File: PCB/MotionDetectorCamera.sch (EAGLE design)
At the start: 163 parts, among them J1 S-MOUNT-LENS-HOLDER, J2 MINI-USB-JACK, Q1 PMOS-NEXPERIA-SOT1220, Q2 PMOS-NEXPERIA-SOT1220, Q3 PMOS-NEXPERIA-SOT1220, U1 TI-TPS6280XYKAR, U10 TI-TPS22919DCK, U11 TI-TPS22919DCK, U12 STM-STM32F730, U13 MICROCHIP-MIC550X, U14 TI-MSP430FR2422IRHL, U15 TI-SN74AXC4T774RSV, U16 TI-TPS22919DCK, U17 DIODESINC-DT1446-04V-7, U18 TI-SN74LVC1G126, U19 PANASONIC-EKMB110711X, U2 TI-TPS6280XYKAR, U3 TI-TPS63805YFFR, U4 LATTICE-ICE40HX4K-BG121, U5 ON-AR0330CS1C12SPKA0, U6 ALLIANCE-AS4C8M16MSA-6BIN, U7 MAXIM-MAX40203ANS+T, U8 TI-TPS22919DCK, U9 MICROSD-SOCKET, X1 SITIME-SIT8021, X2 SITIME-SIT8021, X3 EPSON-MC-306

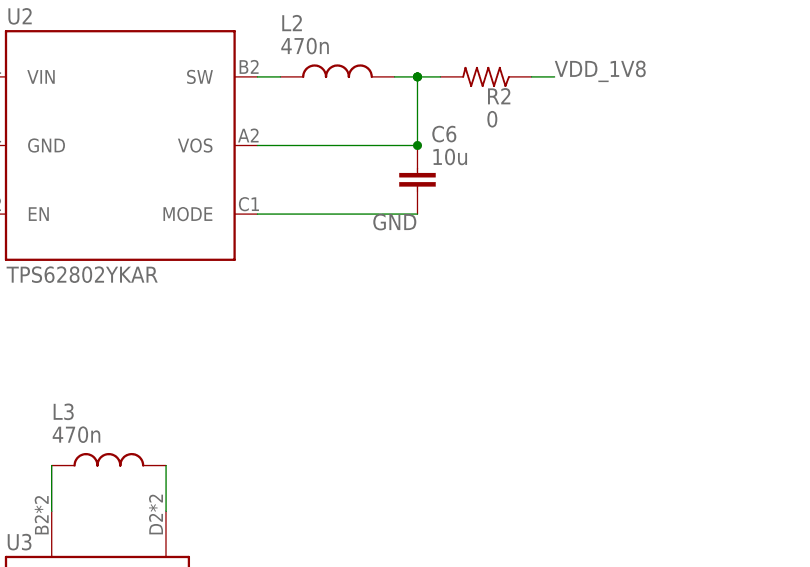
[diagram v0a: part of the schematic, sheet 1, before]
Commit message: Bump 1.8V rail up to 1.9V, so that it's easier to meet the SD card Vih in 3.3V mode
Vih(2.8V) = 0.625*VDD = .625*2.8 = 1.75 V =>
    50mV away from 1.8V rail
    150mV away from 1.9V rail
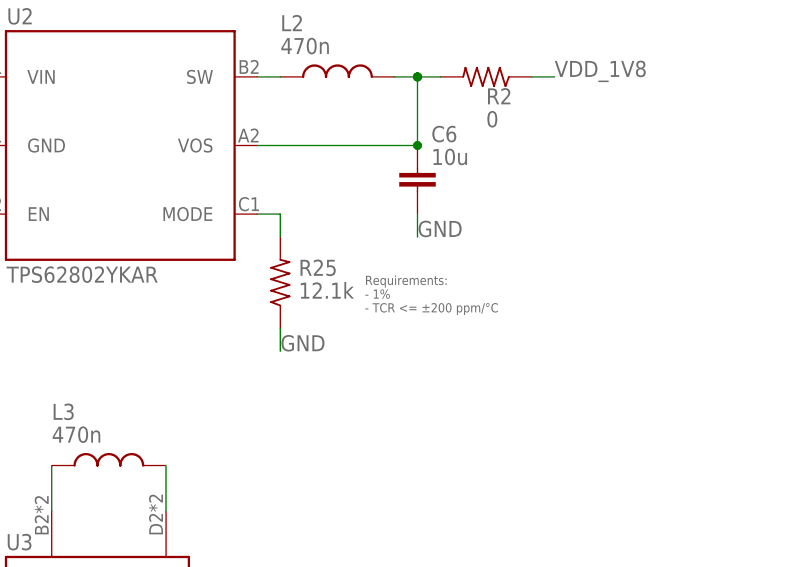
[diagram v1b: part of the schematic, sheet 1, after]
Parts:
- added R25: 12.1k, EagleLibrary:RESISTOR0402
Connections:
- new net N$21: R25.2, U2.MODE
- net GND: now also R25.1; no longer U2.MODE
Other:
- note added: "Requirements: - 1% - TCR <= ±200 ppm/°C"
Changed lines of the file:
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@@
 <attribute name="PN" value="GRM155R61H104KE19D"/>
+</part>
+<part name="R25" library="EagleLibrary" deviceset="RESISTOR" device="0402" value="12.1k">
+<attribute name="MFG" value="Walsin"/>
+<attribute name="PN" value="WR04X1212FTL"/>
 </part>
 </parts>
@@
 <text x="172.974" y="25.146" size="1.016" layer="95" align="top-left">Derated to meet suggested
 1uF @ 5.5V bias</text>
+<text x="179.578" y="257.302" size="1.016" layer="95" align="top-left">Requirements:
+- 1%
+- TCR &lt;= ±200 ppm/°C</text>
 </plain>
 <instances>
@@
 <attribute name="VALUE" x="134.366" y="22.479" size="1.778" layer="96"/>
 <attribute name="MFG" x="114.3" y="30.48" size="1.778" layer="96" display="off"/>
+</instance>
+<instance part="R25" gate="G$1" x="170.18" y="256.54" smashed="yes" rot="R90">
+<attribute name="NAME" x="172.212" y="257.302" size="1.778" layer="95"/>
+<attribute name="VALUE" x="172.212" y="254.762" size="1.778" layer="96"/>
+<attribute name="MFG" x="170.18" y="256.54" size="1.778" layer="96" rot="R90" display="off"/>
+<attribute name="PN" x="170.18" y="256.54" size="1.778" layer="96" rot="R90" display="off"/>
 </instance>
 </instances>
@@
 <wire x1="167.64" y1="309.88" x2="185.42" y2="309.88" width="0.1524" layer="91"/>
 <pinref part="C3" gate="G$1" pin="2"/>
-</segment>
-<segment>
-<pinref part="U2" gate="G$1" pin="MODE"/>
-<label x="185.42" y="264.16" size="1.778" layer="95" align="top-right"/>
-<wire x1="167.64" y1="264.16" x2="185.42" y2="264.16" width="0.1524" layer="91"/>
-<pinref part="C6" gate="G$1" pin="2"/>
 </segment>
 <segment>
@@
 <wire x1="132.08" y1="20.32" x2="132.08" y2="17.78" width="0.1524" layer="91"/>
 <label x="132.08" y="17.78" size="1.778" layer="95" align="bottom-right"/>
+</segment>
+<segment>
+<pinref part="C6" gate="G$1" pin="2"/>
+<wire x1="185.42" y1="264.16" x2="185.42" y2="261.62" width="0.1524" layer="91"/>
+<label x="185.42" y="261.62" size="1.778" layer="95"/>
+</segment>
+<segment>
+<pinref part="R25" gate="G$1" pin="1"/>
+<wire x1="170.18" y1="251.46" x2="170.18" y2="248.92" width="0.1524" layer="91"/>
+<label x="170.18" y="248.92" size="1.778" layer="95"/>
 </segment>
 </net>
@@
 </segment>
 </net>
+<net name="N$21" class="0">
+<segment>
+<pinref part="U2" gate="G$1" pin="MODE"/>
+<wire x1="167.64" y1="264.16" x2="170.18" y2="264.16" width="0.1524" layer="91"/>
+<pinref part="R25" gate="G$1" pin="2"/>
+<wire x1="170.18" y1="264.16" x2="170.18" y2="261.62" width="0.1524" layer="91"/>
+</segment>
+</net>

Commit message: Rename nets 1V8 -> 1V9
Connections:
- net VDD_1V8 renamed VDD_1V9
- net VDD_1V8_IMG renamed VDD_1V9_IMG
- net VDD_1V8_IMG_EN renamed VDD_1V9_IMG_EN
- net VDD_1V8_SD renamed VDD_1V9_SD
- net VDD_1V8_STM renamed VDD_1V9_STM
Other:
- note added: "VDD_1V9"
- note added: "VDD_1V9_IMG"
- note added: "VDD_1V9_STM - Battery: VDD_1V9_STM = HiZ - USB: VDD_1V9_STM = VDD_1V9"
- note added: "VDD_A - Battery: VDD_A = VDD_BAT - USB: VDD_A = 1V9"
- note removed: "VDD_1V8"
- note removed: "VDD_1V8_IMG"
- note removed: "VDD_1V8_STM - Battery: VDD_1V8_STM = HiZ - USB: VDD_1V8_STM = VDD_1V8"
- note removed: "VDD_A - Battery: VDD_A = VDD_BAT - USB: VDD_A = 1V8"
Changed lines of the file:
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@@
 through a via at a different
 layer."</text>
-<text x="12.7" y="81.28" size="3.81" layer="95" align="top-left">VDD_1V8_STM
-- Battery:  VDD_1V8_STM = HiZ
-- USB:      VDD_1V8_STM = VDD_1V8</text>
+<text x="12.7" y="81.28" size="3.81" layer="95" align="top-left">VDD_1V9_STM
+- Battery:  VDD_1V9_STM = HiZ
+- USB:      VDD_1V9_STM = VDD_1V9</text>
 <text x="12.7" y="411.48" size="3.81" layer="95" align="top-left">VDD_A
 - Battery:  VDD_A = VDD_BAT
-- USB:      VDD_A = 1V8</text>
+- USB:      VDD_A = 1V9</text>
 <text x="12.7" y="373.38" size="3.81" layer="95" align="top-left">VDD_B
 - Battery:  VDD_B = HiZ / VDD_BAT
@@
 - USB:      VDD_B = VDD_USB</text>
 <text x="12.7" y="330.2" size="3.81" layer="95" align="top-left">VDD_1V2</text>
-<text x="12.7" y="281.94" size="3.81" layer="95" align="top-left">VDD_1V8</text>
+<text x="12.7" y="281.94" size="3.81" layer="95" align="top-left">VDD_1V9</text>
 <text x="12.7" y="218.44" size="3.81" layer="95" align="top-left">VDD_2V8</text>
 <text x="99.568" y="422.402" size="1.016" layer="95" align="top-left">This PFET serves 2 purposes for the battery power supply:
@@
 <text x="103.886" y="379.984" size="1.016" layer="95" align="top-left">Capacitor helps minimize reverse current spikes
 when battery is inserted with reverse polarity.</text>
-<text x="12.7" y="172.72" size="3.81" layer="95" align="top-left">VDD_1V8_IMG</text>
+<text x="12.7" y="172.72" size="3.81" layer="95" align="top-left">VDD_1V9_IMG</text>
 <text x="12.7" y="142.24" size="3.81" layer="95" align="top-left">VDD_2V8_IMG</text>
 <text x="12.7" y="111.76" size="3.81" layer="95" align="top-left">VDD_2V8_SD</text>
@@
 </segment>
 </net>
-<net name="VDD_1V8" class="0">
+<net name="VDD_1V9" class="0">
 <segment>
 <pinref part="R2" gate="G$1" pin="1"/>
@@
 </segment>
 </net>
-<net name="VDD_1V8_STM" class="0">
+<net name="VDD_1V9_STM" class="0">
 <segment>
 <wire x1="160.02" y1="76.2" x2="162.56" y2="76.2" width="0.1524" layer="91"/>
@@
 </segment>
 </net>
-<net name="VDD_1V8_IMG" class="0">
+<net name="VDD_1V9_IMG" class="0">
 <segment>
 <wire x1="160.02" y1="167.64" x2="162.56" y2="167.64" width="0.1524" layer="91"/>
@@
 </segment>
 </net>
-<net name="VDD_1V8_IMG_EN" class="0">
+<net name="VDD_1V9_IMG_EN" class="0">
 <segment>
 <wire x1="137.16" y1="160.02" x2="134.62" y2="160.02" width="0.1524" layer="91"/>
@@
 </segment>
 </net>
-<net name="VDD_1V8" class="0">
+<net name="VDD_1V9" class="0">
 <segment>
 <pinref part="U15" gate="G$1" pin="VCCB"/>
@@
 </segment>
 </net>
-<net name="VDD_1V8_IMG_EN" class="0">
+<net name="VDD_1V9_IMG_EN" class="0">
 <segment>
 <wire x1="35.56" y1="78.74" x2="33.02" y2="78.74" width="0.1524" layer="91"/>
@@
 </busses>
 <nets>
-<net name="VDD_1V8" class="0">
+<net name="VDD_1V9" class="0">
 <segment>
 <pinref part="C17" gate="G$1" pin="1"/>
@@
 </busses>
 <nets>
-<net name="VDD_1V8_IMG" class="0">
+<net name="VDD_1V9_IMG" class="0">
 <segment>
 <pinref part="U5" gate="A" pin="VDD_IO"/>
@@
 </busses>
 <nets>
-<net name="VDD_1V8" class="0">
+<net name="VDD_1V9" class="0">
 <segment>
 <pinref part="C43" gate="G$1" pin="1"/>
@@
 </busses>
 <nets>
-<net name="VDD_1V8_SD" class="0">
+<net name="VDD_1V9_SD" class="0">
 <segment>
 <pinref part="R22" gate="G$1" pin="2"/>
@@
 </segment>
 </net>
-<net name="VDD_1V8_STM" class="0">
+<net name="VDD_1V9_STM" class="0">
 <segment>
 <pinref part="U12" gate="K" pin="VDD_C5"/>

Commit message: Comments
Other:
- note added: "We're using 1.9V instead of 1.8V purely to help meet the Vih of the SD card when it's in 3.3V mode. In 3.3V mode, the SD card is supposed to be supplied 3.3V signals, but the ICE40 gives it 1.9V signals instead. We're doing this because we haven't found a good method of switching the signal voltage without introducing capacitance on the signalling lines (which can greatly impact the 100MHz high-s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"
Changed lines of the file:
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@@
 - 1%
 - TCR &lt;= ±200 ppm/°C</text>
+<text x="12.7" y="274.32" size="1.016" layer="95" align="top-left">We're using 1.9V instead of 1.8V purely to
+help meet the Vih of the SD card when it's
+in 3.3V mode.
+In 3.3V mode, the SD card is supposed to
+be supplied 3.3V signals, but the ICE40
+gives it 1.9V signals instead. We're doing
+this because we haven't found a good
+method of switching the signal voltage
+without introducing capacitance on the
+signalling lines (which can greatly impact
+the 100MHz high-speed mode).</text>
 </plain>
 <instances>

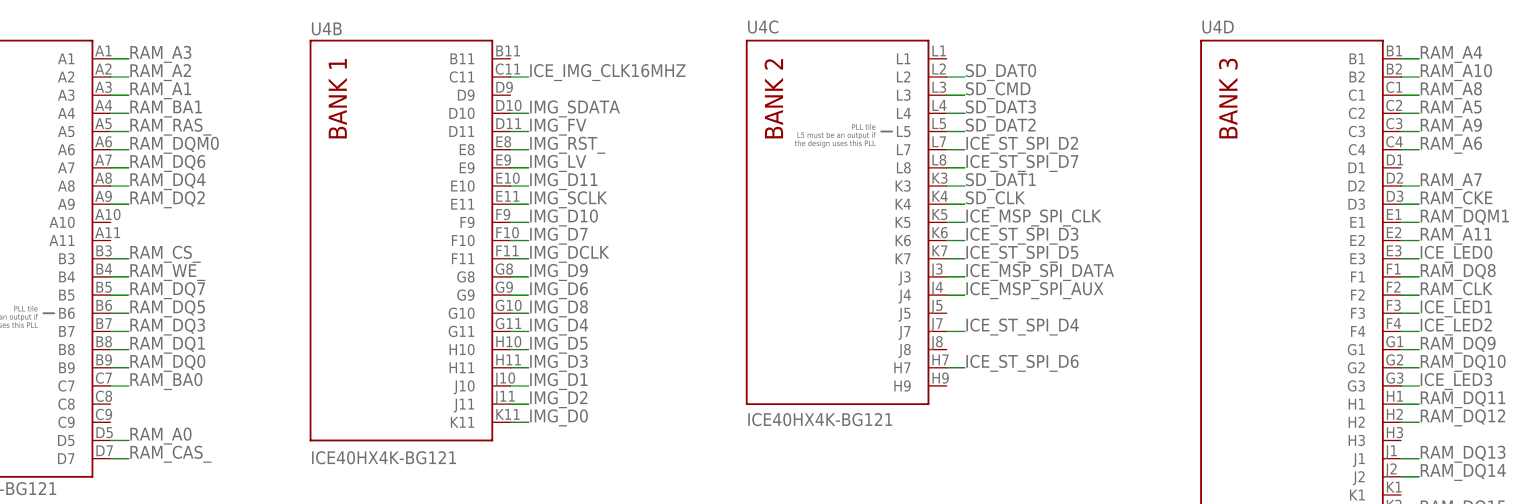
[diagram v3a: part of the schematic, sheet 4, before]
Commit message: Fixed ICE40 PLL tile pins so that they're either unused, or output-only
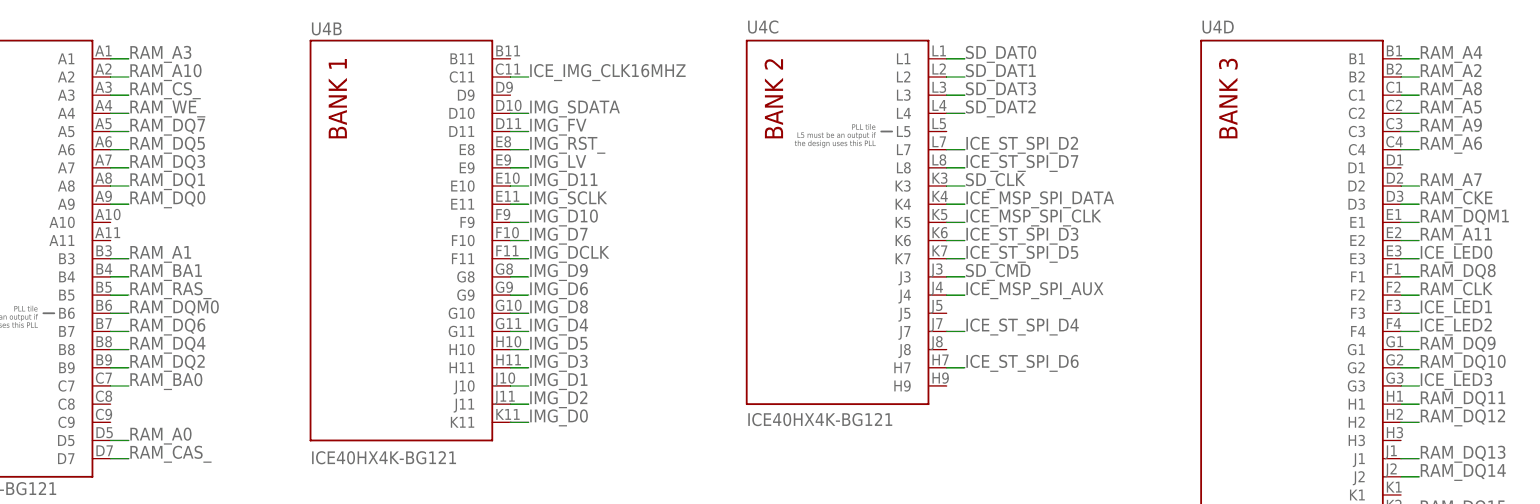
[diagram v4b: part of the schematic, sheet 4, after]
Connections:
- net ICE_MSP_SPI_DATA: now also U4C.K4; no longer U4C.J3
- net RAM_A1: now also U4A.B3; no longer U4A.A3
- net RAM_A10: now also U4A.A2; no longer U4D.B2
- net RAM_A2: now also U4D.B2; no longer U4A.A2
- net RAM_BA1: now also U4A.B4; no longer U4A.A4
- net RAM_CS_: now also U4A.A3; no longer U4A.B3
- net RAM_DQ0: now also U4A.A9; no longer U4A.B9
- net RAM_DQ1: now also U4A.A8; no longer U4A.B8
- net RAM_DQ2: now also U4A.B9; no longer U4A.A9
- net RAM_DQ3: now also U4A.A7; no longer U4A.B7
- net RAM_DQ4: now also U4A.B8; no longer U4A.A8
- net RAM_DQ5: now also U4A.A6; no longer U4A.B6
- net RAM_DQ6: now also U4A.B7; no longer U4A.A7
- net RAM_DQ7: now also U4A.A5; no longer U4A.B5
- net RAM_DQM0: now also U4A.B6; no longer U4A.A6
- net RAM_RAS_: now also U4A.B5; no longer U4A.A5
- net RAM_WE_: now also U4A.A4; no longer U4A.B4
- net SD_CLK: now also U4C.K3; no longer U4C.K4
- net SD_CMD: now also U4C.J3; no longer U4C.L3
- net SD_DAT0: now also U4C.L1; no longer U4C.L2
- net SD_DAT1: now also U4C.L2; no longer U4C.K3
- net SD_DAT2: now also U4C.L4; no longer U4C.L5
- net SD_DAT3: now also U4C.L3; no longer U4C.L4

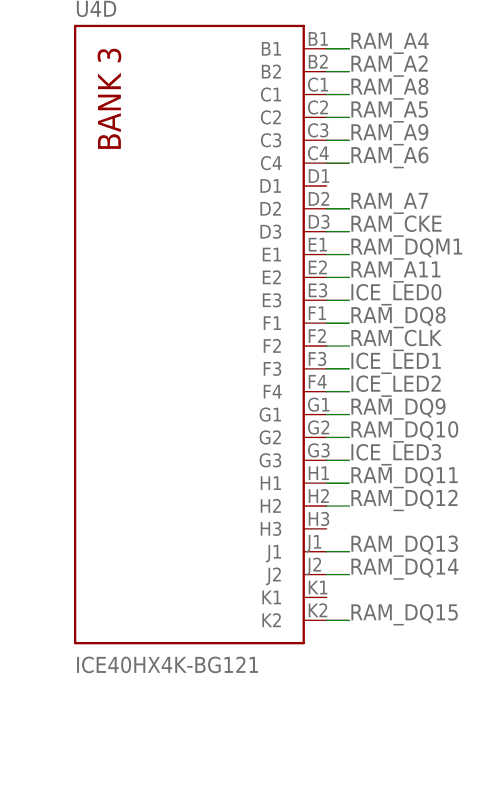
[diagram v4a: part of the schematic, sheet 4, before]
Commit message: Compact wires going to RAM now that we no longer have an A12 net (ball G1)
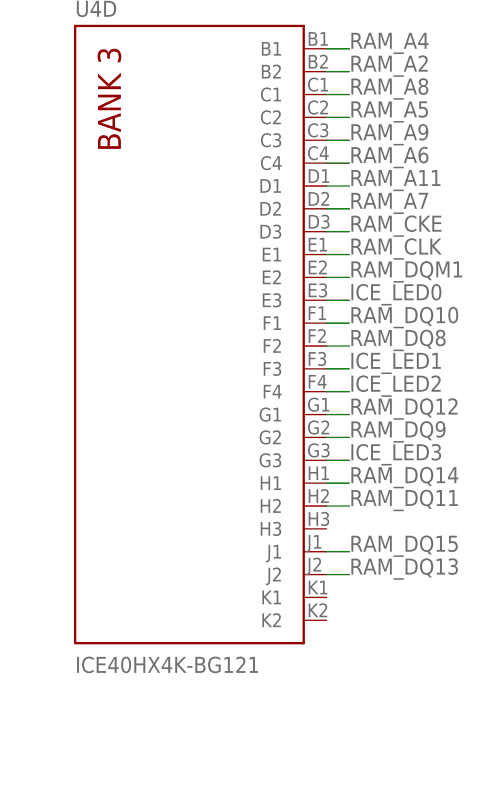
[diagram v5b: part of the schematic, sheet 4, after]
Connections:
- net RAM_A11: now also U4D.D1; no longer U4D.E2
- net RAM_CLK: now also U4D.E1; no longer U4D.F2
- net RAM_DQ10: now also U4D.F1; no longer U4D.G2
- net RAM_DQ11: now also U4D.H2; no longer U4D.H1
- net RAM_DQ12: now also U4D.G1; no longer U4D.H2
- net RAM_DQ13: now also U4D.J2; no longer U4D.J1
- net RAM_DQ14: now also U4D.H1; no longer U4D.J2
- net RAM_DQ15: now also U4D.J1; no longer U4D.K2
- net RAM_DQ8: now also U4D.F2; no longer U4D.F1
- net RAM_DQ9: now also U4D.G2; no longer U4D.G1
- net RAM_DQM1: now also U4D.E2; no longer U4D.E1
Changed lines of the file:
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@@
-</segment>
-</net>
-<net name="RAM_CLK" class="0">
-<segment>
-<pinref part="U4" gate="D" pin="F2"/>
-<wire x1="213.36" y1="33.02" x2="215.9" y2="33.02" width="0.1524" layer="91"/>
-<label x="215.9" y="33.02" size="1.778" layer="95"/>
-</segment>
-</net>
-<net name="RAM_DQM1" class="0">
-<segment>
-<pinref part="U4" gate="D" pin="E1"/>
-<wire x1="213.36" y1="43.18" x2="215.9" y2="43.18" width="0.1524" layer="91"/>
-<label x="215.9" y="43.18" size="1.778" layer="95"/>
 </segment>
 </net>
@@
 <label x="35.56" y="63.5" size="1.778" layer="95"/>
 <pinref part="U4" gate="A" pin="A2"/>
-</segment>
-</net>
-<net name="RAM_A11" class="0">
-<segment>
-<pinref part="U4" gate="D" pin="E2"/>
-<wire x1="213.36" y1="40.64" x2="215.9" y2="40.64" width="0.1524" layer="91"/>
-<label x="215.9" y="40.64" size="1.778" layer="95"/>
-</segment>
-</net>
-<net name="RAM_DQ8" class="0">
-<segment>
-<pinref part="U4" gate="D" pin="F1"/>
-<wire x1="213.36" y1="35.56" x2="215.9" y2="35.56" width="0.1524" layer="91"/>
-<label x="215.9" y="35.56" size="1.778" layer="95"/>
-</segment>
-</net>
-<net name="RAM_DQ9" class="0">
-<segment>
-<pinref part="U4" gate="D" pin="G1"/>
-<wire x1="213.36" y1="25.4" x2="215.9" y2="25.4" width="0.1524" layer="91"/>
-<label x="215.9" y="25.4" size="1.778" layer="95"/>
-</segment>
-</net>
-<net name="RAM_DQ10" class="0">
-<segment>
-<pinref part="U4" gate="D" pin="G2"/>
-<wire x1="213.36" y1="22.86" x2="215.9" y2="22.86" width="0.1524" layer="91"/>
-<label x="215.9" y="22.86" size="1.778" layer="95"/>
-</segment>
-</net>
-<net name="RAM_DQ11" class="0">
-<segment>
-<pinref part="U4" gate="D" pin="H1"/>
-<wire x1="213.36" y1="17.78" x2="215.9" y2="17.78" width="0.1524" layer="91"/>
-<label x="215.9" y="17.78" size="1.778" layer="95"/>
-</segment>
-</net>
-<net name="RAM_DQ12" class="0">
-<segment>
-<pinref part="U4" gate="D" pin="H2"/>
-<wire x1="213.36" y1="15.24" x2="215.9" y2="15.24" width="0.1524" layer="91"/>
-<label x="215.9" y="15.24" size="1.778" layer="95"/>
-</segment>
-</net>
-<net name="RAM_DQ13" class="0">
-<segment>
-<pinref part="U4" gate="D" pin="J1"/>
-<wire x1="213.36" y1="10.16" x2="215.9" y2="10.16" width="0.1524" layer="91"/>
-<label x="215.9" y="10.16" size="1.778" layer="95"/>
-</segment>
-</net>
-<net name="RAM_DQ14" class="0">
-<segment>
-<pinref part="U4" gate="D" pin="J2"/>
-<wire x1="213.36" y1="7.62" x2="215.9" y2="7.62" width="0.1524" layer="91"/>
-<label x="215.9" y="7.62" size="1.778" layer="95"/>
-</segment>
-</net>
-<net name="RAM_DQ15" class="0">
-<segment>
-<pinref part="U4" gate="D" pin="K2"/>
-<wire x1="213.36" y1="2.54" x2="215.9" y2="2.54" width="0.1524" layer="91"/>
-<label x="215.9" y="2.54" size="1.778" layer="95"/>
 </segment>
 </net>
@@
 </segment>
 </net>
+<net name="RAM_A11" class="0">
+<segment>
+<wire x1="213.36" y1="50.8" x2="215.9" y2="50.8" width="0.1524" layer="91"/>
+<label x="215.9" y="50.8" size="1.778" layer="95"/>
+<pinref part="U4" gate="D" pin="D1"/>
+</segment>
+</net>
+<net name="RAM_DQM1" class="0">
+<segment>
+<wire x1="213.36" y1="40.64" x2="215.9" y2="40.64" width="0.1524" layer="91"/>
+<label x="215.9" y="40.64" size="1.778" layer="95"/>
+<pinref part="U4" gate="D" pin="E2"/>
+</segment>
+</net>
+<net name="RAM_CLK" class="0">
+<segment>
+<wire x1="213.36" y1="43.18" x2="215.9" y2="43.18" width="0.1524" layer="91"/>
+<label x="215.9" y="43.18" size="1.778" layer="95"/>
+<pinref part="U4" gate="D" pin="E1"/>
+</segment>
+</net>
+<net name="RAM_DQ8" class="0">
+<segment>
+<wire x1="213.36" y1="33.02" x2="215.9" y2="33.02" width="0.1524" layer="91"/>
+<label x="215.9" y="33.02" size="1.778" layer="95"/>
+<pinref part="U4" gate="D" pin="F2"/>
+</segment>
+</net>
+<net name="RAM_DQ10" class="0">
+<segment>
+<wire x1="213.36" y1="35.56" x2="215.9" y2="35.56" width="0.1524" layer="91"/>
+<label x="215.9" y="35.56" size="1.778" layer="95"/>
+<pinref part="U4" gate="D" pin="F1"/>
+</segment>
+</net>
+<net name="RAM_DQ9" class="0">
+<segment>
+<wire x1="213.36" y1="22.86" x2="215.9" y2="22.86" width="0.1524" layer="91"/>
+<label x="215.9" y="22.86" size="1.778" layer="95"/>
+<pinref part="U4" gate="D" pin="G2"/>
+</segment>
+</net>
+<net name="RAM_DQ12" class="0">
+<segment>
+<wire x1="213.36" y1="25.4" x2="215.9" y2="25.4" width="0.1524" layer="91"/>
+<label x="215.9" y="25.4" size="1.778" layer="95"/>
+<pinref part="U4" gate="D" pin="G1"/>
+</segment>
+</net>
+<net name="RAM_DQ11" class="0">
+<segment>
+<wire x1="213.36" y1="15.24" x2="215.9" y2="15.24" width="0.1524" layer="91"/>
+<label x="215.9" y="15.24" size="1.778" layer="95"/>
+<pinref part="U4" gate="D" pin="H2"/>
+</segment>
+</net>
+<net name="RAM_DQ14" class="0">
+<segment>
+<wire x1="213.36" y1="17.78" x2="215.9" y2="17.78" width="0.1524" layer="91"/>
+<label x="215.9" y="17.78" size="1.778" layer="95"/>
+<pinref part="U4" gate="D" pin="H1"/>
+</segment>
+</net>
+<net name="RAM_DQ13" class="0">
+<segment>
+<wire x1="213.36" y1="7.62" x2="215.9" y2="7.62" width="0.1524" layer="91"/>
+<label x="215.9" y="7.62" size="1.778" layer="95"/>
+<pinref part="U4" gate="D" pin="J2"/>
+</segment>
+</net>
+<net name="RAM_DQ15" class="0">
+<segment>
+<wire x1="213.36" y1="10.16" x2="215.9" y2="10.16" width="0.1524" layer="91"/>
+<label x="215.9" y="10.16" size="1.778" layer="95"/>
+<pinref part="U4" gate="D" pin="J1"/>
+</segment>
+</net>

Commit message: Add load switch to VDD_USB to limit inrush current
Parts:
- added C78, C79, C80, C81, C82: 2.2u, EagleLibrary:CAPACITOR0402
- added U20: TI-TPS22919DCK, EagleLibrary:TI-TPS22919DCK
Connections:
- new net VDD_USB_IN: C78.1, C79.1, C80.1, C81.1, C82.1, FB1.P$2, U20.EN, U20.VIN
- net GND: now also C78.2, C79.2, C80.2, C81.2, C82.2, U20.GND
- net VDD_USB: now also U20.VOUT; no longer FB1.P$2
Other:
- note added: "Ceff = 1uF @ 5.5V bias"
- note added: "Using load switch purely for its soft-start behavior, to limit USB inrush current"
- note removed: "Derated to meet suggested 1uF @ 5.5V bias"
- moved on the sheet: C1, C10, C2, C3, C4, C44, C45, C5, C6, C7, C8, C9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
